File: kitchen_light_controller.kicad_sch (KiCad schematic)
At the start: 9 parts, among them J1 1935161, J2 1935161, J3 1935161, J4 1935161, J5 1935161, U1 SC0915, U2 VND7140AJTR, U3 VND7140AJTR

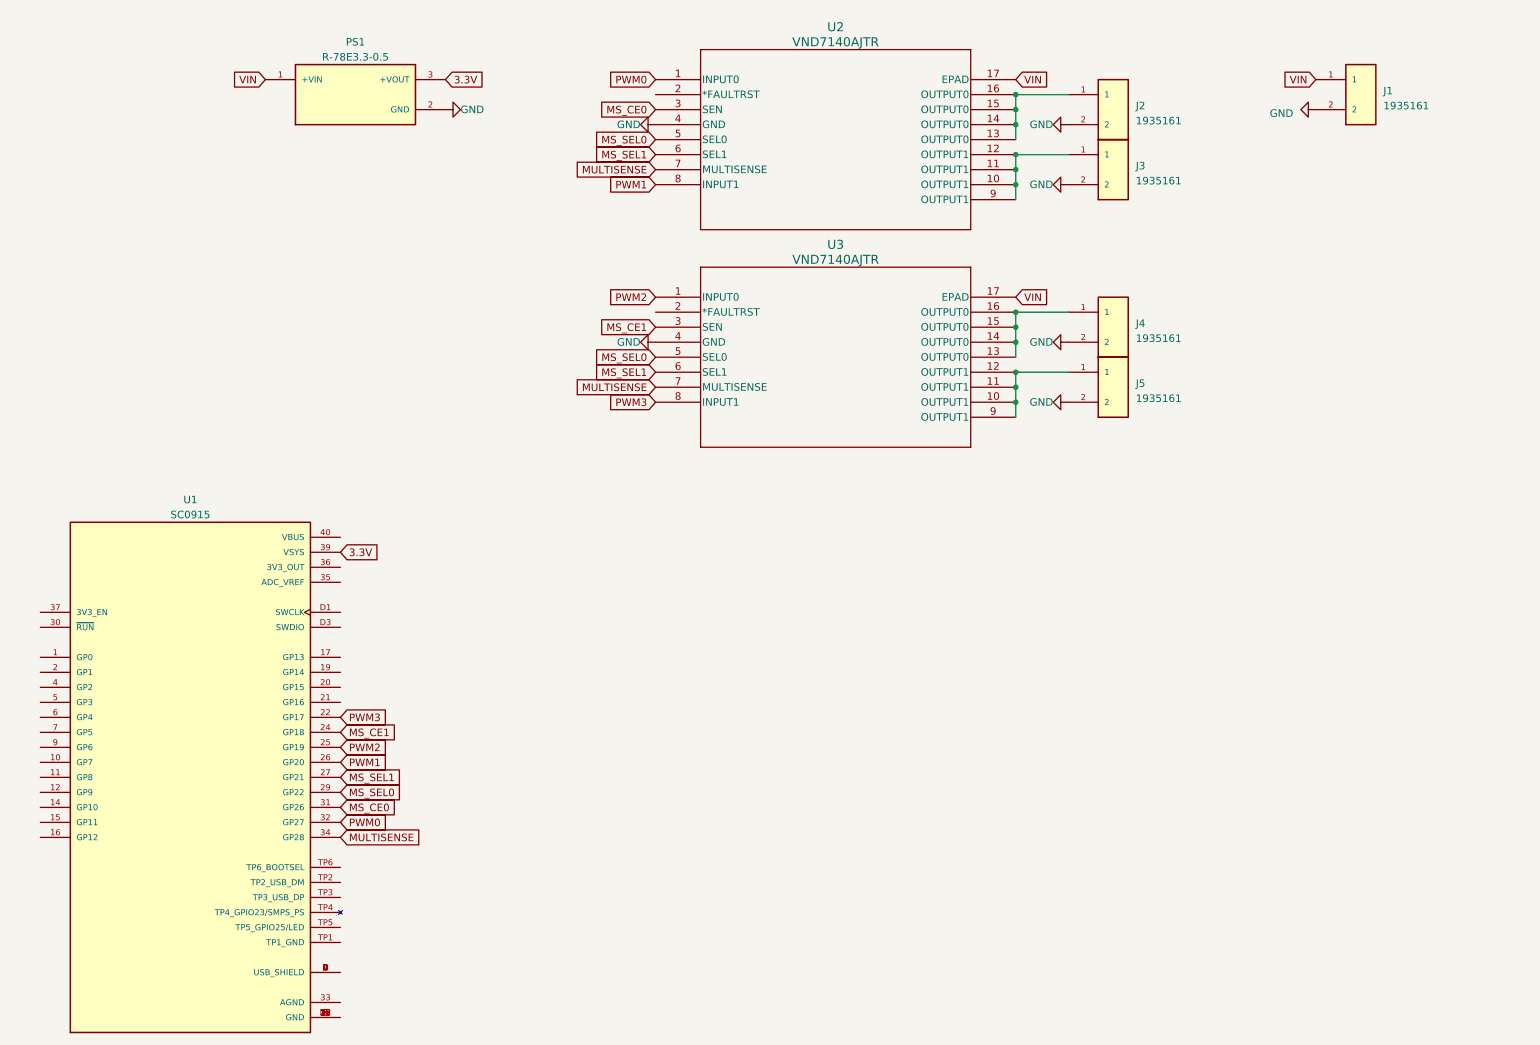
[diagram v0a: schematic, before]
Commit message: Reduced to dual channel (Single IC)
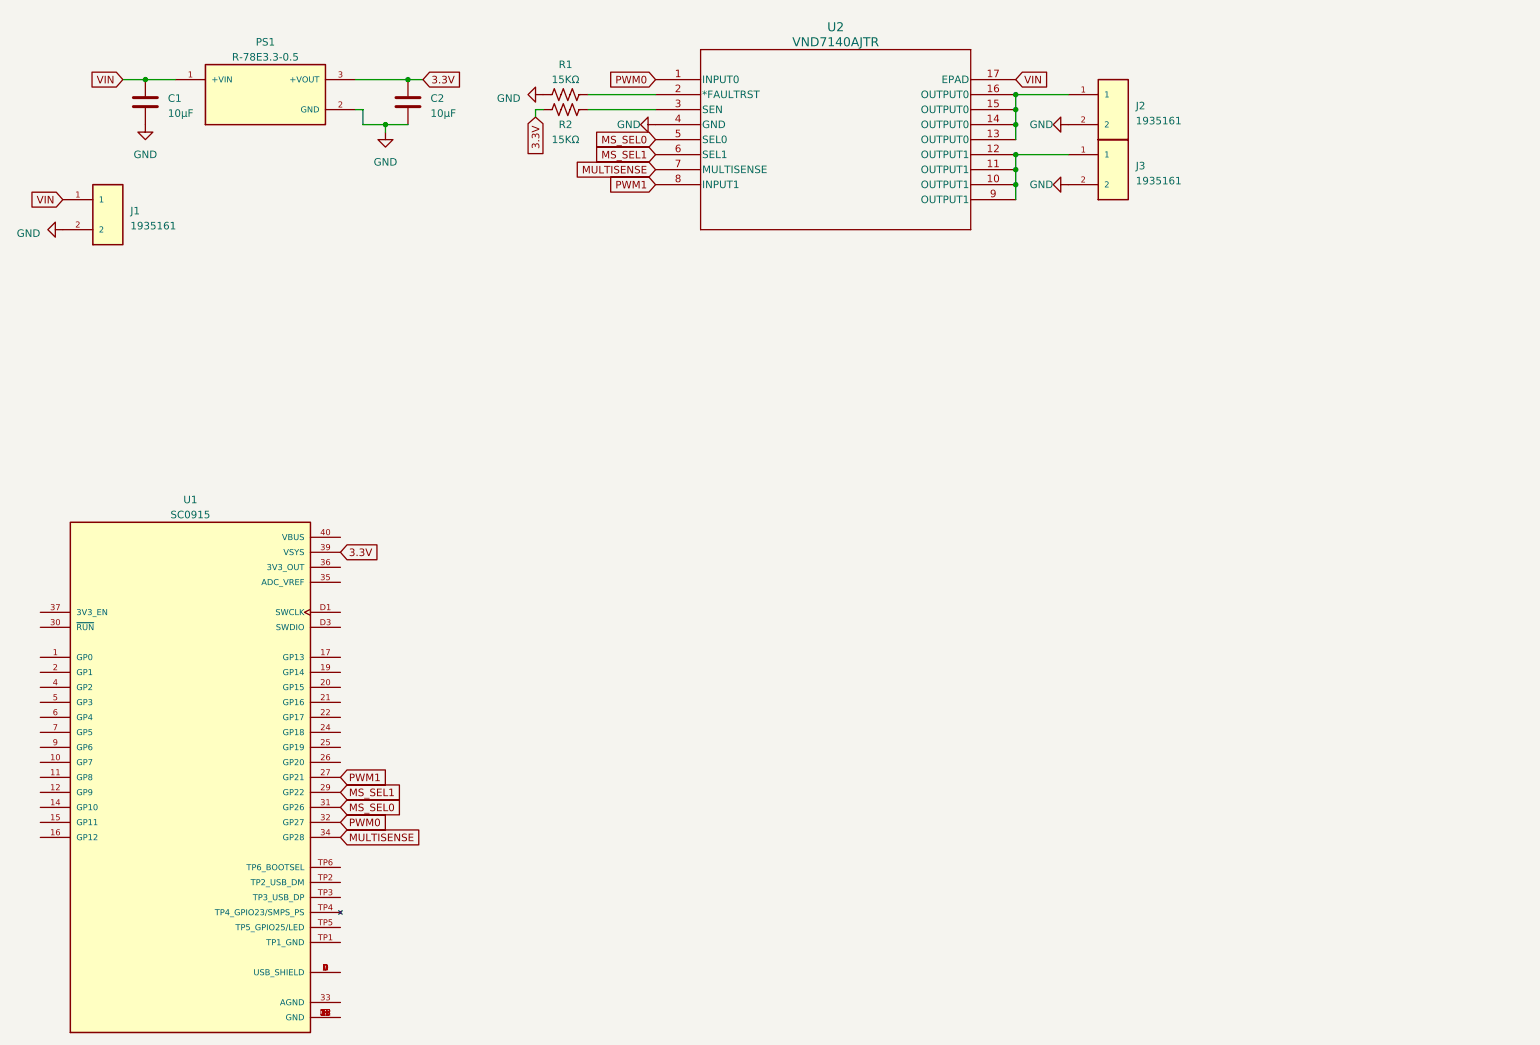
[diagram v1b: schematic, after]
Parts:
- removed J4, J5: 1935161, Raspberry Pi Pico:PHOENIX_1935161, symbol Phoenix Connect 1935161:1935161
- removed U3: VND7140AJTR, Raspberry Pi Pico:POWERSSO16_STM, symbol STM VND7140AJTR:VND7140AJTR
- added C1, C2: 10μF, Capacitor_SMD:C_0805_2012Metric_Pad1.18x1.45mm_HandSolder, symbol Device:C
- added R1, R2: 15KΩ, Resistor_SMD:R_0201_0603Metric_Pad0.64x0.40mm_HandSolder, symbol Device:R_US
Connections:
- net 3.3V: now also C2.1, R2.1
- net GND: now also C1.2, C2.2, R1.1
- net MS_SEL0: now also U1.31 (GP26); no longer U1.29 (GP22)
- net MS_SEL1: now also U1.29 (GP22); no longer U1.27 (GP21)
- net PWM1: now also U1.27 (GP21); no longer U1.26 (GP20)
- net VIN: now also C1.1
- net at U2.2 (*FAULTRST): now also R1.2
- net MS_CE0: no longer names the net of U2.3 (SEN)
- net MS_CE0: now also R2.2; no longer U1.31 (GP26)
- net MS_CE1: no longer names the net of U1.24 (GP18)
- net PWM2: no longer names the net of U1.25 (GP19)
- net PWM3: no longer names the net of U1.22 (GP17)
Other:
- moved on the sheet: J1, PS1

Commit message: Added debounced control switches
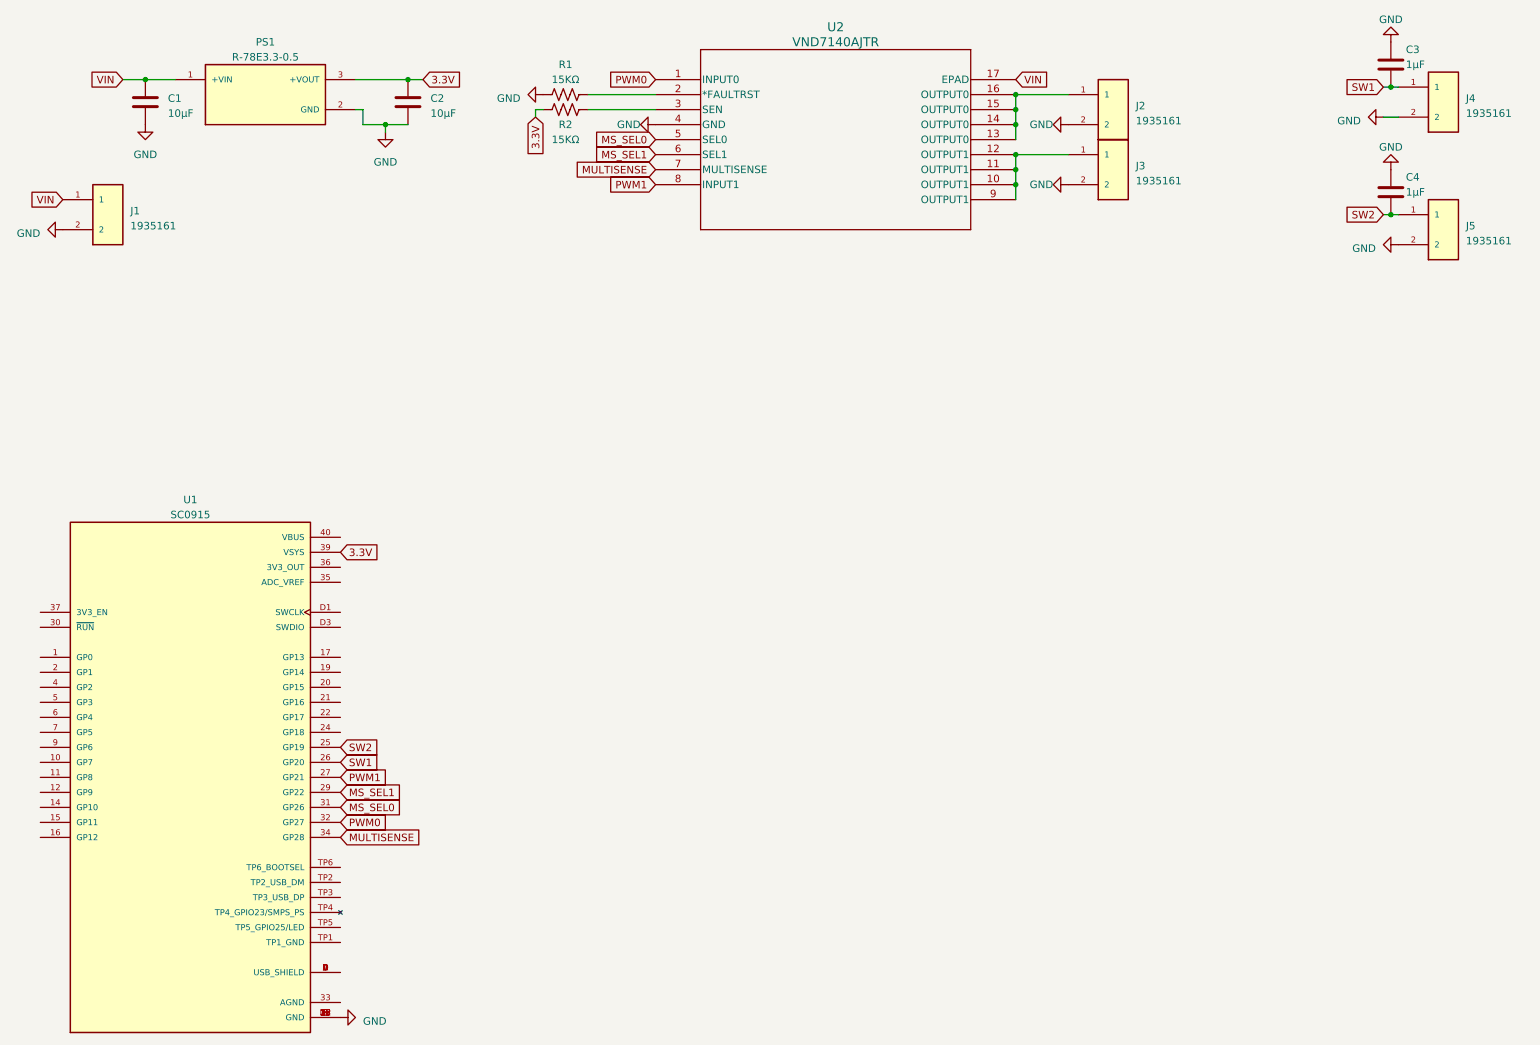
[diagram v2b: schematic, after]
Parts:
- added C3, C4: 1μF, Capacitor_SMD:C_0805_2012Metric_Pad1.18x1.45mm_HandSolder, symbol Device:C
- added J4, J5: 1935161, Raspberry Pi Pico:PHOENIX_1935161, symbol Phoenix Connect 1935161:1935161
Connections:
- net GND: now also U1.13 (GND), U1.18 (GND), U1.23 (GND), U1.28 (GND), U1.3 (GND), U1.38 (GND), U1.8 (GND), U1.D2 (GND), C3.1, C4.1, J4.2, J5.2
- net SW2: now reaches U1.25 (GP19)
- net SW2: now also C4.2, J5.1
- net SW1: now reaches U1.26 (GP20)
- net SW1: now also C3.2, J4.1

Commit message: Added analog motion sensor header
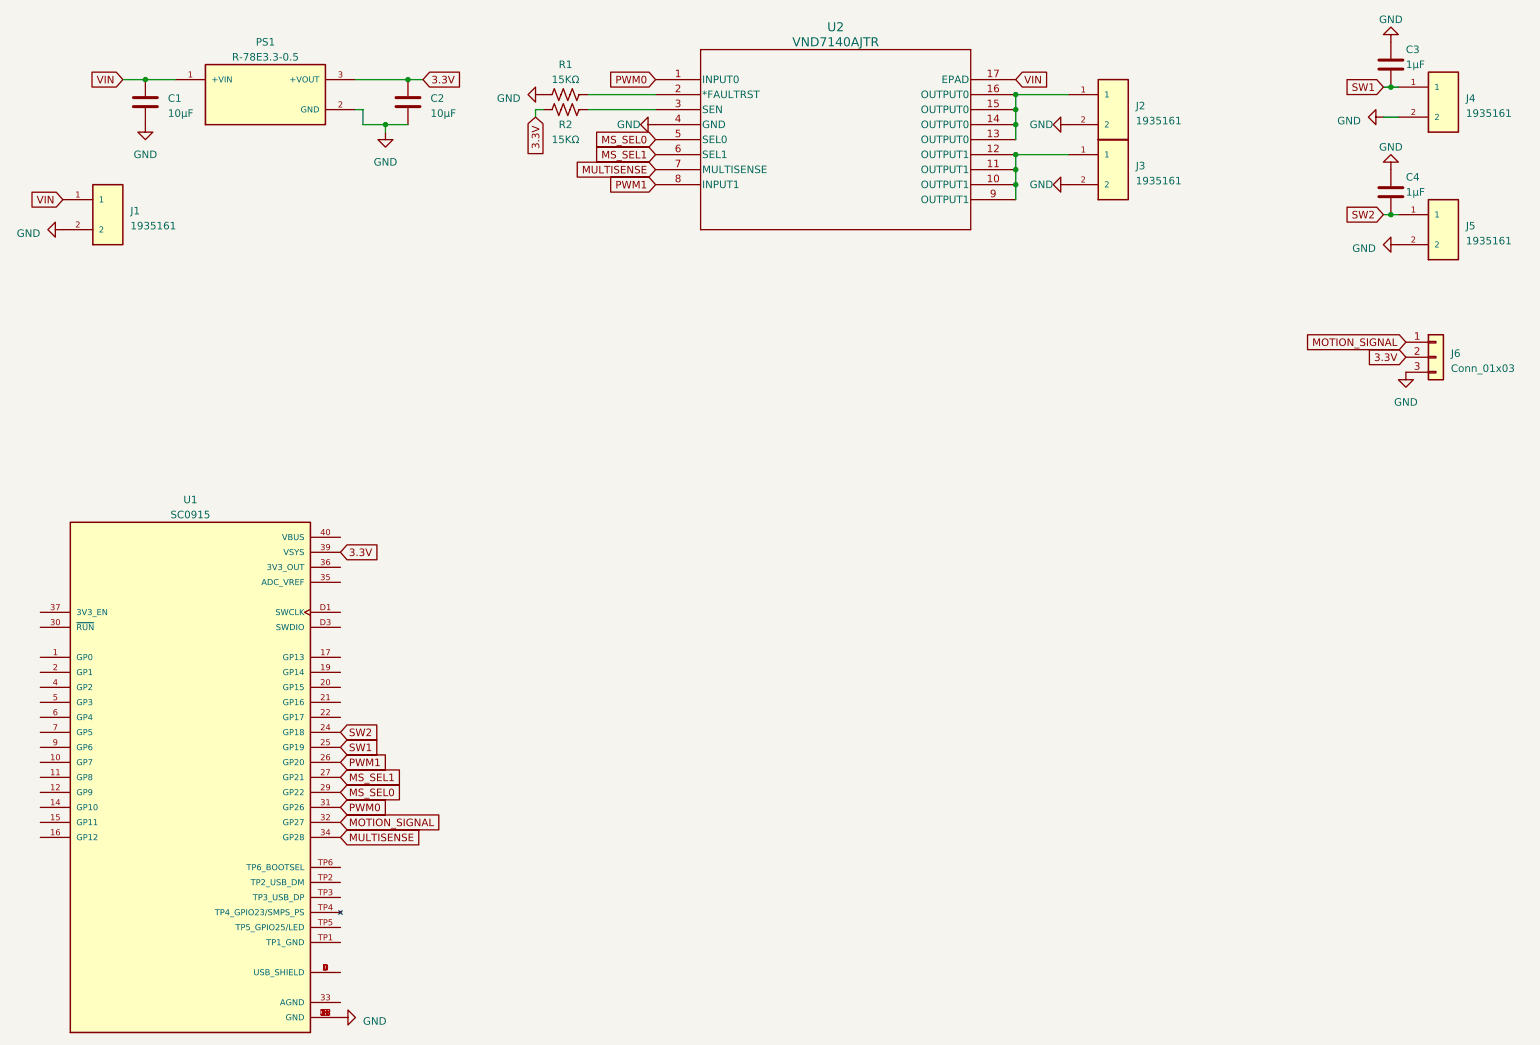
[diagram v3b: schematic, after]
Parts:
- added J6: Conn_01x03, Connector_PinHeader_2.54mm:PinHeader_1x03_P2.54mm_Vertical, symbol Connector_Generic:Conn_01x03
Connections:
- net 3.3V: now also J6.2 (Pin_2)
- net GND: now also J6.3 (Pin_3)
- net MS_SEL0: now also U1.29 (GP22); no longer U1.31 (GP26)
- net MS_SEL1: now also U1.27 (GP21); no longer U1.29 (GP22)
- net PWM0: now also U1.31 (GP26); no longer U1.32 (GP27)
- net PWM1: now also U1.26 (GP20); no longer U1.27 (GP21)
- net SW1: now also U1.25 (GP19); no longer U1.26 (GP20)
- net SW2: now also U1.24 (GP18); no longer U1.25 (GP19)
- new net MOTION_SIGNAL: J6.1 (Pin_1), U1.32 (GP27)
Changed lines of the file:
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@@
     )
   )
-  (global_label "MS_SEL1" (shape input) (at 76.2 146.05 0) (fields_autoplaced)
+  (global_label "MS_SEL1" (shape input) (at 76.2 143.51 0) (fields_autoplaced)
+    (effects (font (size 1.27 1.27)) (justify left))
+    (property "Intersheetrefs" "${INTERSHEET_REFS}" (at 87.3304 143.51 0)
+      (effects (font (size 1.27 1.27)) (justify left) hide)
+    )
+  )
+  (global_label "PWM1" (shape input) (at 76.2 140.97 0) (fields_autoplaced)
+    (effects (font (size 1.27 1.27)) (justify left))
+    (property "Intersheetrefs" "${INTERSHEET_REFS}" (at 84.4881 140.97 0)
+      (effects (font (size 1.27 1.27)) (justify left) hide)
+    )
+  )
+  (global_label "SW2" (shape input) (at 252.73 48.26 180) (fields_autoplaced)
+    (effects (font (size 1.27 1.27)) (justify right))
+    (property "Intersheetrefs" "${INTERSHEET_REFS}" (at 245.9538 48.26 0)
+      (effects (font (size 1.27 1.27)) (justify right) hide)
+    )
+  )
+  (global_label "MS_SEL0" (shape input) (at 76.2 146.05 0) (fields_autoplaced)
     (effects (font (size 1.27 1.27)) (justify left))
     (property "Intersheetrefs" "${INTERSHEET_REFS}" (at 87.3304 146.05 0)
@@
     )
   )
-  (global_label "PWM1" (shape input) (at 76.2 143.51 0) (fields_autoplaced)
-    (effects (font (size 1.27 1.27)) (justify left))
-    (property "Intersheetrefs" "${INTERSHEET_REFS}" (at 84.4881 143.51 0)
-      (effects (font (size 1.27 1.27)) (justify left) hide)
-    )
-  )
-  (global_label "SW2" (shape input) (at 252.73 48.26 180) (fields_autoplaced)
-    (effects (font (size 1.27 1.27)) (justify right))
-    (property "Intersheetrefs" "${INTERSHEET_REFS}" (at 245.9538 48.26 0)
-      (effects (font (size 1.27 1.27)) (justify right) hide)
-    )
-  )
-  (global_label "MS_SEL0" (shape input) (at 76.2 148.59 0) (fields_autoplaced)
-    (effects (font (size 1.27 1.27)) (justify left))
-    (property "Intersheetrefs" "${INTERSHEET_REFS}" (at 87.3304 148.59 0)
-      (effects (font (size 1.27 1.27)) (justify left) hide)
-    )
-  )
   (global_label "PWM1" (shape input) (at 129.54 43.18 180) (fields_autoplaced)
     (effects (font (size 1.27 1.27)) (justify right))
@@
     )
   )
-  (global_label "PWM0" (shape input) (at 76.2 151.13 0) (fields_autoplaced)
-    (effects (font (size 1.27 1.27)) (justify left))
-    (property "Intersheetrefs" "${INTERSHEET_REFS}" (at 84.4881 151.13 0)
-      (effects (font (size 1.27 1.27)) (justify left) hide)
-    )
-  )
-  (global_label "SW1" (shape input) (at 76.2 140.97 0) (fields_autoplaced)
-    (effects (font (size 1.27 1.27)) (justify left))
-    (property "Intersheetrefs" "${INTERSHEET_REFS}" (at 82.9762 140.97 0)
+  (global_label "PWM0" (shape input) (at 76.2 148.59 0) (fields_autoplaced)
+    (effects (font (size 1.27 1.27)) (justify left))
+    (property "Intersheetrefs" "${INTERSHEET_REFS}" (at 84.4881 148.59 0)
+      (effects (font (size 1.27 1.27)) (justify left) hide)
+    )
+  )
+  (global_label "SW1" (shape input) (at 76.2 138.43 0) (fields_autoplaced)
+    (effects (font (size 1.27 1.27)) (justify left))
+    (property "Intersheetrefs" "${INTERSHEET_REFS}" (at 82.9762 138.43 0)
       (effects (font (size 1.27 1.27)) (justify left) hide)
     )
@@
     )
   )
+  (global_label "3.3V" (shape input) (at 256.54 72.39 180) (fields_autoplaced)
+    (effects (font (size 1.27 1.27)) (justify right))
+    (property "Intersheetrefs" "${INTERSHEET_REFS}" (at 249.5218 72.39 0)
+      (effects (font (size 1.27 1.27)) (justify right) hide)
+    )
+  )
   (global_label "VIN" (shape input) (at 190.5 25.4 0) (fields_autoplaced)
     (effects (font (size 1.27 1.27)) (justify left))
@@
     )
   )
+  (global_label "MOTION_SIGNAL" (shape input) (at 256.54 69.85 180) (fields_autoplaced)
+    (effects (font (size 1.27 1.27)) (justify right))
+    (property "Intersheetrefs" "${INTERSHEET_REFS}" (at 239.1198 69.85 0)
+      (effects (font (size 1.27 1.27)) (justify right) hide)
+    )
+  )
   (global_label "SW1" (shape input) (at 252.73 26.67 180) (fields_autoplaced)
     (effects (font (size 1.27 1.27)) (justify right))
@@
     )
   )
-  (global_label "SW2" (shape input) (at 76.2 138.43 0) (fields_autoplaced)
-    (effects (font (size 1.27 1.27)) (justify left))
-    (property "Intersheetrefs" "${INTERSHEET_REFS}" (at 82.9762 138.43 0)
+  (global_label "MOTION_SIGNAL" (shape input) (at 76.2 151.13 0) (fields_autoplaced)
+    (effects (font (size 1.27 1.27)) (justify left))
+    (property "Intersheetrefs" "${INTERSHEET_REFS}" (at 93.6202 151.13 0)
+      (effects (font (size 1.27 1.27)) (justify left) hide)
+    )
+  )
+  (global_label "SW2" (shape input) (at 76.2 135.89 0) (fields_autoplaced)
+    (effects (font (size 1.27 1.27)) (justify left))
+    (property "Intersheetrefs" "${INTERSHEET_REFS}" (at 82.9762 135.89 0)
       (effects (font (size 1.27 1.27)) (justify left) hide)
     )
@@
     )
   )
+  (symbol (lib_id "Connector_Generic:Conn_01x03") (at 261.62 72.39 0) (unit 1)
+    (in_bom yes) (on_board yes) (dnp no)
+    (property "Reference" "J6" (at 264.16 71.755 0)
+      (effects (font (size 1.27 1.27)) (justify left))
+    )
+    (property "Value" "Conn_01x03" (at 264.16 74.295 0)
+      (effects (font (size 1.27 1.27)) (justify left))
+    )
+    (property "Footprint" "Connector_PinHeader_2.54mm:PinHeader_1x03_P2.54mm_Vertical" (at 261.62 72.39 0)
+      (effects (font (size 1.27 1.27)) hide)
+    )
+    (property "Datasheet" "~" (at 261.62 72.39 0)
+      (effects (font (size 1.27 1.27)) hide)
+    )
+    (pin "1")
+    (pin "2")
+    (pin "3")
+    (instances
+      (project "kitchen_light_controller"
+        (path "/b7dbd127-2340-4bb0-b060-ce4a2230bf8a"
+          (reference "J6") (unit 1)
+        )
+      )
+    )
+  )
   (symbol (lib_id "power:GND") (at 252.73 31.75 270) (unit 1)
     (in_bom yes) (on_board yes) (dnp no) (fields_autoplaced)
@@
         )
       )
+    )
+  )
+  (symbol (lib_id "power:GND") (at 256.54 74.93 0) (unit 1)
+    (in_bom yes) (on_board yes) (dnp no) (fields_autoplaced)
+    (property "Reference" "#PWR013" (at 256.54 81.28 0)
+      (effects (font (size 1.27 1.27)) hide)
+    )
+    (property "Value" "GND" (at 256.54 80.01 0)
+      (effects (font (size 1.27 1.27)))
+    )
+    (property "Footprint" "" (at 256.54 74.93 0)
+      (effects (font (size 1.27 1.27)) hide)
+    )
+    (property "Datasheet" "" (at 256.54 74.93 0)
+      (effects (font (size 1.27 1.27)) hide)
+    )
+    (pin "1")
+    (instances
+      (project "kitchen_light_controller"
+        (path "/b7dbd127-2340-4bb0-b060-ce4a2230bf8a"
+          (reference "#PWR013") (unit 1)
+        )
+      )
